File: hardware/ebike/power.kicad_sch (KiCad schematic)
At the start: 42 parts, among them IC1 DRV8302, J1 Screw_Terminal_01x02, Q1 TC2117-3.3VEBTR

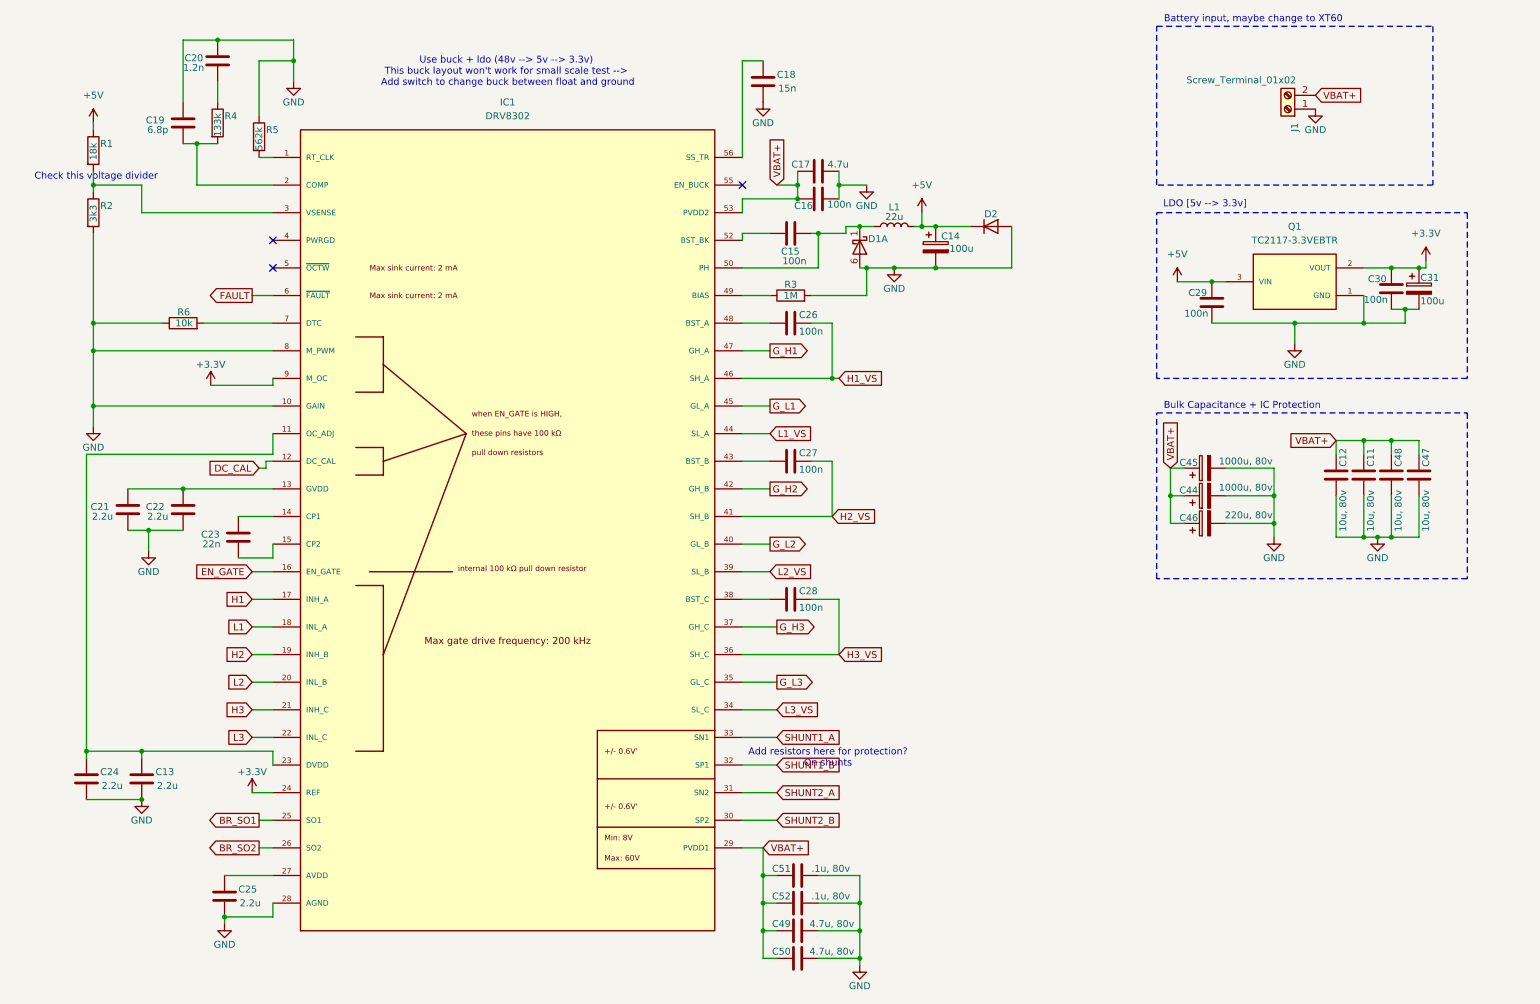
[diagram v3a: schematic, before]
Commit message: Added all peripherals and started modifying power circuitry
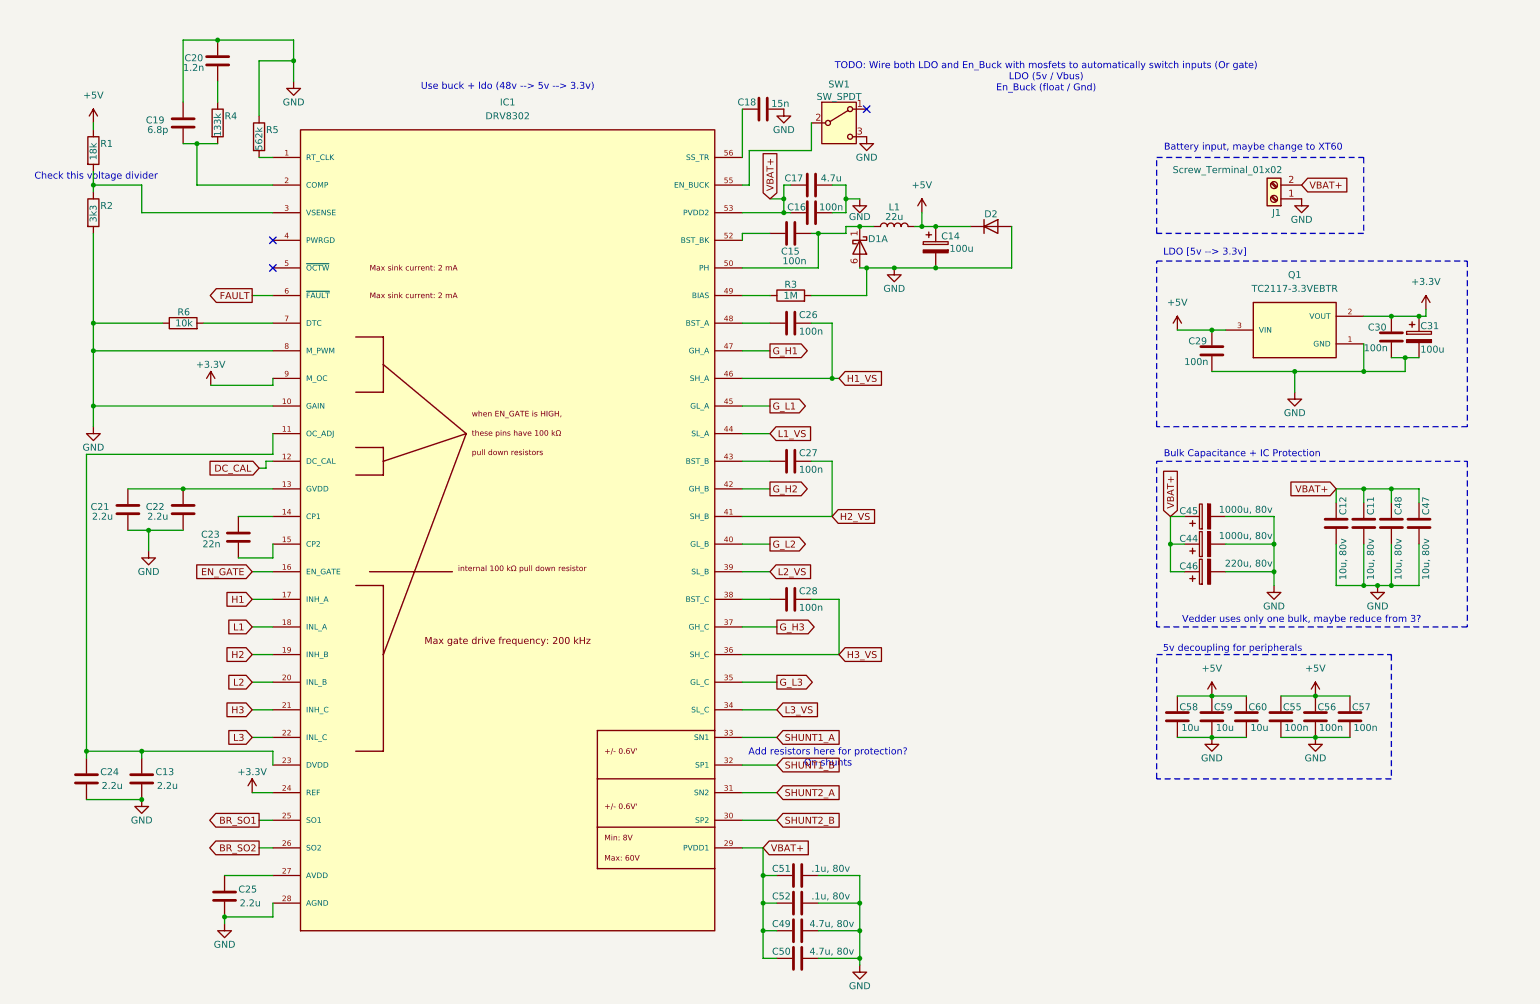
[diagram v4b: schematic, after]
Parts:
- added C55, C56, C57: 100n, symbol Device:C
- added C58, C59, C60: 10u, symbol Device:C
- added SW1: SW_SPDT, symbol Switch:SW_SPDT
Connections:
- net +5V: now also C55.1, C56.1, C57.1, C58.1, C59.1, C60.1
- net AGND: now also C55.2, C56.2, C57.2, C58.2, C59.2, C60.2, SW1.3 (C)
- net at IC1.55 (EN_BUCK): now also SW1.2 (B)
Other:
- note added: "5v decoupling for peripherals"
- note added: "TODO: Wire both LDO and En_Buck with mosfets to automatically switch inputs (Or gate) LDO (5v / Vbus) En_Buck (float / Gnd)"
- note added: "Use buck + ldo (48v --> 5v --> 3.3v)"
- note added: "Vedder uses only one bulk, maybe reduce from 3?"
- note removed: "Use buck + ldo (48v --> 5v --> 3.3v) This buck layout won't work for small scale test --> Add switch to change buck between float and ground"
- moved on the sheet: C11, C12, C16, C17, C18, C29, C30, C31, C44, C45, C46, C47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

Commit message: schematic ready for first review
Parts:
- added D11: LED, symbol Device:LED
- added R40: 100, symbol Device:R
- added SW2: SW_SPDT, symbol Switch:SW_SPDT
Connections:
- net +3.3V: now also D11.2 (A)
- net +5V: now also SW2.1 (A); no longer C29.2, Q1.3 (VIN)
- net AGND: now also R40.1
- new net: D11.1 (K), R40.2
- new net: C29.2, Q1.3 (VIN), SW2.2 (B)
- new net VBUS: SW2.3 (C)
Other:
- note added: "Battery input"
- note added: "change xt60?"
- note removed: "Battery input, maybe change to XT60"
- note removed: "TODO: Wire both LDO and En_Buck with mosfets to automatically switch inputs (Or gate) LDO (5v / Vbus) En_Buck (float / Gnd)"
- moved on the sheet: C11, C12, C29, C30, C31, C44, C45, C46, C47, C48, C55, C56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

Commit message: working through first review, edited Power control a lot
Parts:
- removed C50: 4.7u, 80v, symbol Device:C
- removed C52: .1u, 80v, symbol Device:C
- removed D2: ~, symbol Device:D
- added C62, C63: 2.2u, symbol Device:C
- added R41: 10k, symbol Device:R
- C19: value 6.8p -> 6.8n
- C20: value 1.2n -> 120p
- C44, C45: value 1000u, 80v -> 220u, 80v
- R4: value 133k -> 15k
- R5: value 562k -> 220k
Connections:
- net AGND: now also C62.2, C63.2, R41.2
- net at C13.1, C24.1, IC1.11 (OC_ADJ): now also R41.1; no longer IC1.23 (DVDD)
- net OCTW: now reaches IC1.5 (~{OCTW})
- new net: C62.1, C63.1, IC1.23 (DVDD)
- no-connect marks 3 -> 2
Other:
- note added: "Have very short traces resistor to ground (RT_CLK)"
- note added: "Place one of each cap near DRV VCC pin + peripheral x2, Maybe reduce b/c we alr have 100u bulk on 5v line"
- note added: "TODO: Finish annotating this page"
- note removed: "Add resistors here for protection? On shunts"
- note removed: "Check this voltage divider"
- moved on the sheet: C13, C14, C21, C24, C49, C55, C56, C57, C58, C59, C60, D1A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

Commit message: finished annoation for schematic
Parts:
- C29: value 100n -> 10u
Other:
- note added: "loose polarized cap?"
- note removed: "TODO: Finish annotating this page"
- note removed: "Vedder uses only one bulk, maybe reduce from 3?"
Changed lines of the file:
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@@
 	(rectangle
 		(start 213.36 72.39)
-		(end 270.51 102.87)
+		(end 270.51 101.6)
 		(stroke
 			(width 0)
@@
 		)
 	)
-	(text "Vedder uses only one bulk, maybe reduce from 3?"
-		(exclude_from_sim no)
-		(at 240.03 101.6 0)
-		(effects
-			(font
-				(size 1.27 1.27)
-			)
-		)
-	)
 	(text "Place one of each cap near DRV VCC pin + peripheral x2,\nMaybe reduce b/c we alr have 100u bulk on 5v line"
 		(exclude_from_sim no)
@@
 		)
 	)
-	(text "TODO: Finish annotating this page"
+	(text "loose polarized cap?"
 		(exclude_from_sim no)
-		(at 205.486 22.86 0)
+		(at 265.43 34.29 0)
 		(effects
 			(font
-				(size 2.032 2.032)
+				(size 1.27 1.27)
 			)
 		)
@@
 	(text "LDO [5v --> 3.3v]"
 		(exclude_from_sim no)
-		(at 229.87 35.306 0)
+		(at 213.868 35.052 0)
 		(effects
 			(font
@@
 			)
 		)
-		(property "Value" "100n"
-			(at 226.06 55.372 0)
+		(property "Value" "10u"
+			(at 226.822 55.372 0)
 			(effects
 				(font
@@
 			)
 		)
-		(property "Datasheet" "https://www.digikey.com/en/products/detail/microchip-technology/TC2117-3-3VDBTR/443726"
+		(property "Datasheet" "https://ww1.microchip.com/downloads/aemDocuments/documents/APID/ProductDocuments/DataSheets/21665D.pdf"
 			(at 246.38 49.53 0)
 			(effects

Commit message: minor fixes
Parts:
- removed D1: ~, Package_TO_SOT_SMD:SOT-363_SC-70-6, symbol Diode:SD103ATW
- added D1: D_Schottky, symbol Device:D_Schottky
- C49: value 4.7u, 80v -> 2.2u, 80v
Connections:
- net AGND: now also D1.2 (A)
- net at C15.2, IC1.50 (PH), IC1.51 (PH)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: now also D1.1 (K)
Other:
- note removed: "loose polarized cap?"
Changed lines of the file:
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@@
 		)
 	)
-	(text "loose polarized cap?"
-		(exclude_from_sim no)
-		(at 265.43 34.29 0)
-		(effects
-			(font
-				(size 1.27 1.27)
-			)
-		)
-	)
 	(text "Battery input"
 		(exclude_from_sim no)
@@
 			)
 		)
-		(property "Value" "4.7u, 80v"
+		(property "Value" "2.2u, 80v"
 			(at 166.624 177.8 90)
 			(effects
@@
 	)
 	(symbol
-		(lib_id "Diode:SD103ATW")
-		(at 167.64 60.96 270)
-		(unit 1)
-		(exclude_from_sim no)
-		(in_bom yes)
-		(on_board yes)
-		(dnp no)
-		(property "Reference" "D1"
-			(at 169.164 59.436 90)
-			(effects
-				(font
-					(size 1.27 1.27)
-				)
-				(justify left)
-			)
-		)
-		(property "Value" "~"
-			(at 170.18 61.9124 90)
-			(effects
-				(font
-					(size 1.27 1.27)
-				)
-				(justify left)
-			)
-		)
-		(property "Footprint" "Package_TO_SOT_SMD:SOT-363_SC-70-6"
-			(at 162.56 60.96 0)
-			(effects
-				(font
-					(size 1.27 1.27)
-				)
-				(hide yes)
-			)
-		)
-		(property "Datasheet" "https://www.diodes.com/assets/Datasheets/ds30374.pdf"
-			(at 167.64 60.96 0)
-			(effects
-				(font
-					(size 1.27 1.27)
-				)
-				(hide yes)
-			)
-		)
-		(property "Description" "Schottky Barrier Diode Array, SOT-363"
-			(at 167.64 60.96 0)
-			(effects
-				(font
-					(size 1.27 1.27)
-				)
-				(hide yes)
-			)
-		)
-		(pin "2"
-		)
-		(pin "3"
-		)
-		(pin "4"
-		)
-		(pin "5"
-		)
-		(pin "1"
-		)
-		(pin "6"
-		)
-		(instances
-			(project ""
-				(path "/fbe3366b-3e6e-4322-b4fc-2801645ea115/e63b1961-d904-476f-9eef-e137f6634033"
-					(reference "D1")
-					(unit 1)
-				)
-			)
-		)
-	)
-	(symbol
 		(lib_id "Device:R")
 		(at 26.67 52.07 0)
@@
 		(dnp no)
 		(property "Reference" "C20"
-			(at 43.434 23.622 0)
+			(at 45.212 22.098 0)
 			(effects
 				(font
@@
 		)
 		(property "Value" "120p"
-			(at 43.18 25.4 0)
+			(at 44.196 26.162 0)
 			(effects
 				(font
@@
 					(unit 1)
 				)
+			)
+		)
+	)
+	(symbol
+		(lib_id "Device:D_Schottky")
+		(at 167.64 60.96 270)
+		(unit 1)
+		(exclude_from_sim no)
+		(in_bom yes)
+		(on_board yes)
+		(dnp no)
+		(property "Reference" "D1"
+			(at 169.164 59.436 90)
+			(effects
+				(font
+					(size 1.27 1.27)
+				)
+				(justify left)
+			)
+		)
+		(property "Value" "D_Schottky"
+			(at 169.164 61.722 90)
+			(effects
+				(font
+					(size 1.27 1.27)
+				)
+				(justify left)
+			)
+		)
+		(property "Footprint" ""
+			(at 167.64 60.96 0)
+			(effects
+				(font
+					(size 1.27 1.27)
+				)
+				(hide yes)
+			)
+		)
+		(property "Datasheet" "~"
+			(at 167.64 60.96 0)
+			(effects
+				(font
+					(size 1.27 1.27)
+				)
+				(hide yes)
+			)
+		)
+		(property "Description" "Schottky diode"
+			(at 167.64 60.96 0)
+			(effects
+				(font
+					(size 1.27 1.27)
+				)
+				(hide yes)
+			)
+		)
+		(pin "2"
+		)
+		(pin "1"
+		)
+		(instances
+			(project "ebike"
+				(path "/fbe3366b-3e6e-4322-b4fc-2801645ea115/e63b1961-d904-476f-9eef-e137f6634033"
+					(reference "D1")
+					(unit 1)
+				)
